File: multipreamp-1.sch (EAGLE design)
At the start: 132 parts, among them Q1 J201, Q2 J201, Q3 J201, Q4 J201, Q5 2N5088, Q6 J201, Q7 J201, Q8 J201

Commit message: Adicao de filtros RC na alimentacao (esquematico e layout)
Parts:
- added C43: (no value), rcl:CPOL-EUE2.5-6
- added R49, R50: (no value), rcl:R-US_0207/7
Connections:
- new net 9V_1: C3.1, C37.1, C6.+, Q5.C, Q8.D, R23.A, R29.A, R31.1, R49.2, R50.1
- new net N$44: JP+.1, R49.1
- net GND: now also C43.-
- net V+: now also C43.+, R50.2; no longer C3.1, C37.1, C6.+, JP+.1, Q5.C, Q8.D, R23.A, R29.A, R31.1
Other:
- moved on the sheet: C26, C27, C3, C38, C6, C7, JP+, JP-, Q6, R40, R7

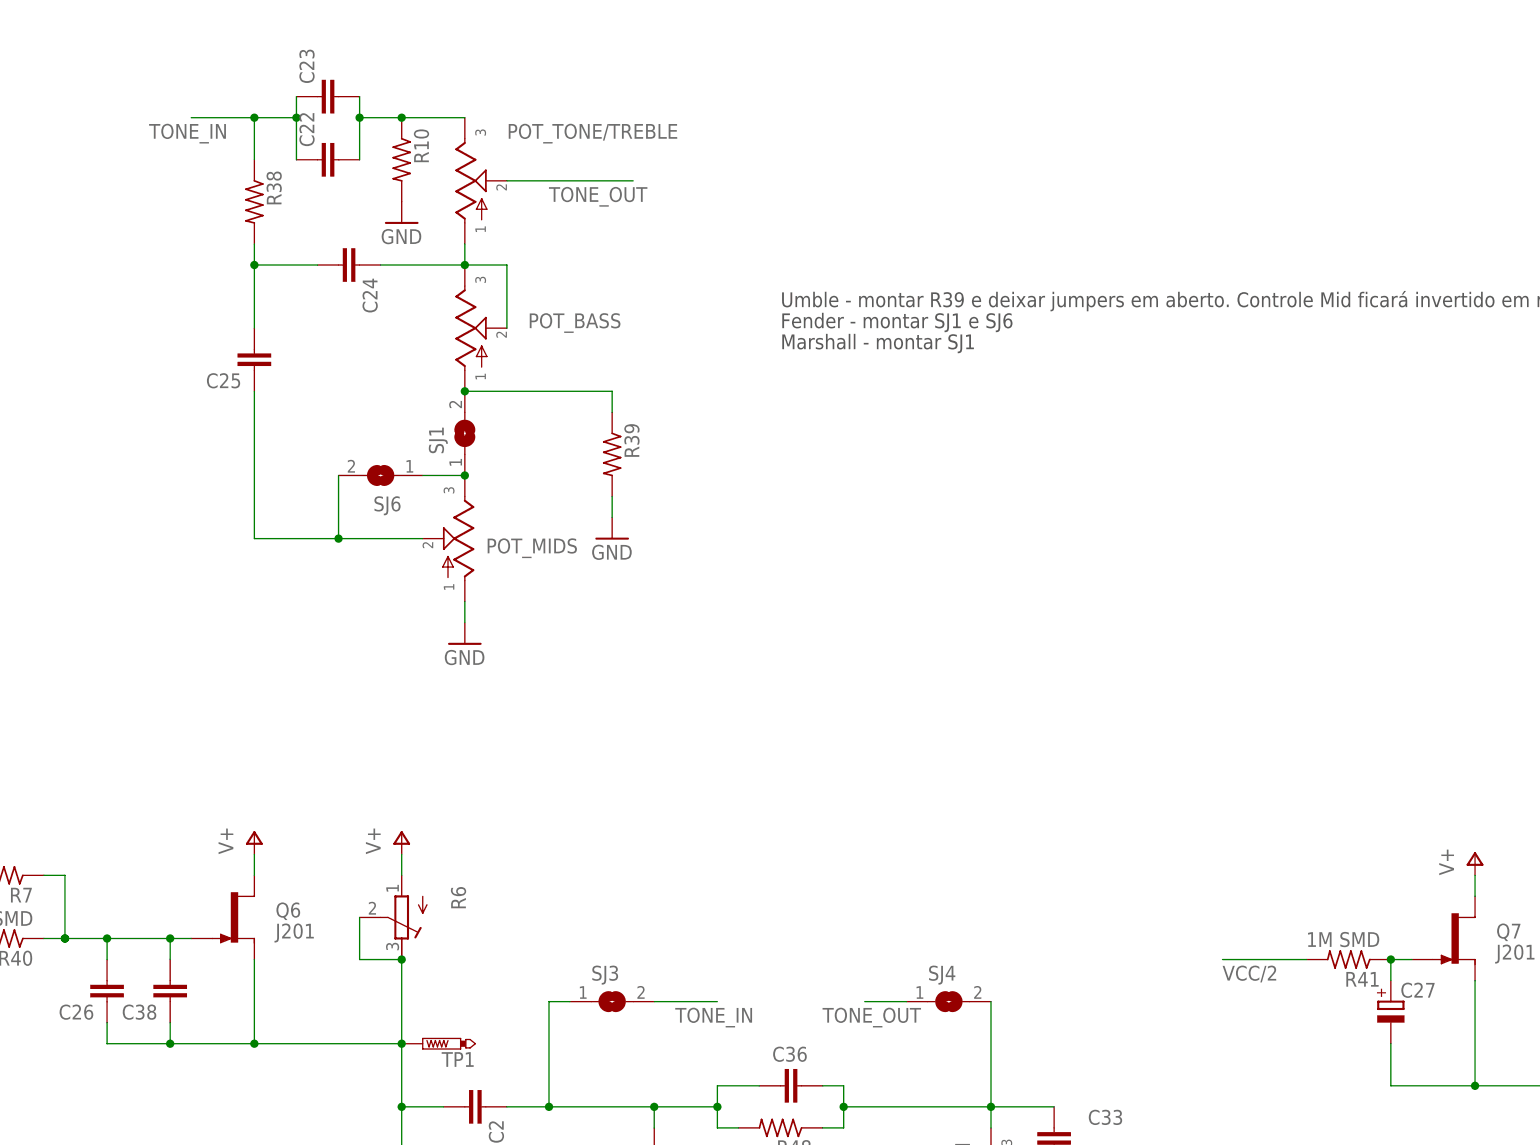
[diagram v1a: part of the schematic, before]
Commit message: Alteracao no layout - troca de posicao entre pots de agudos e graves
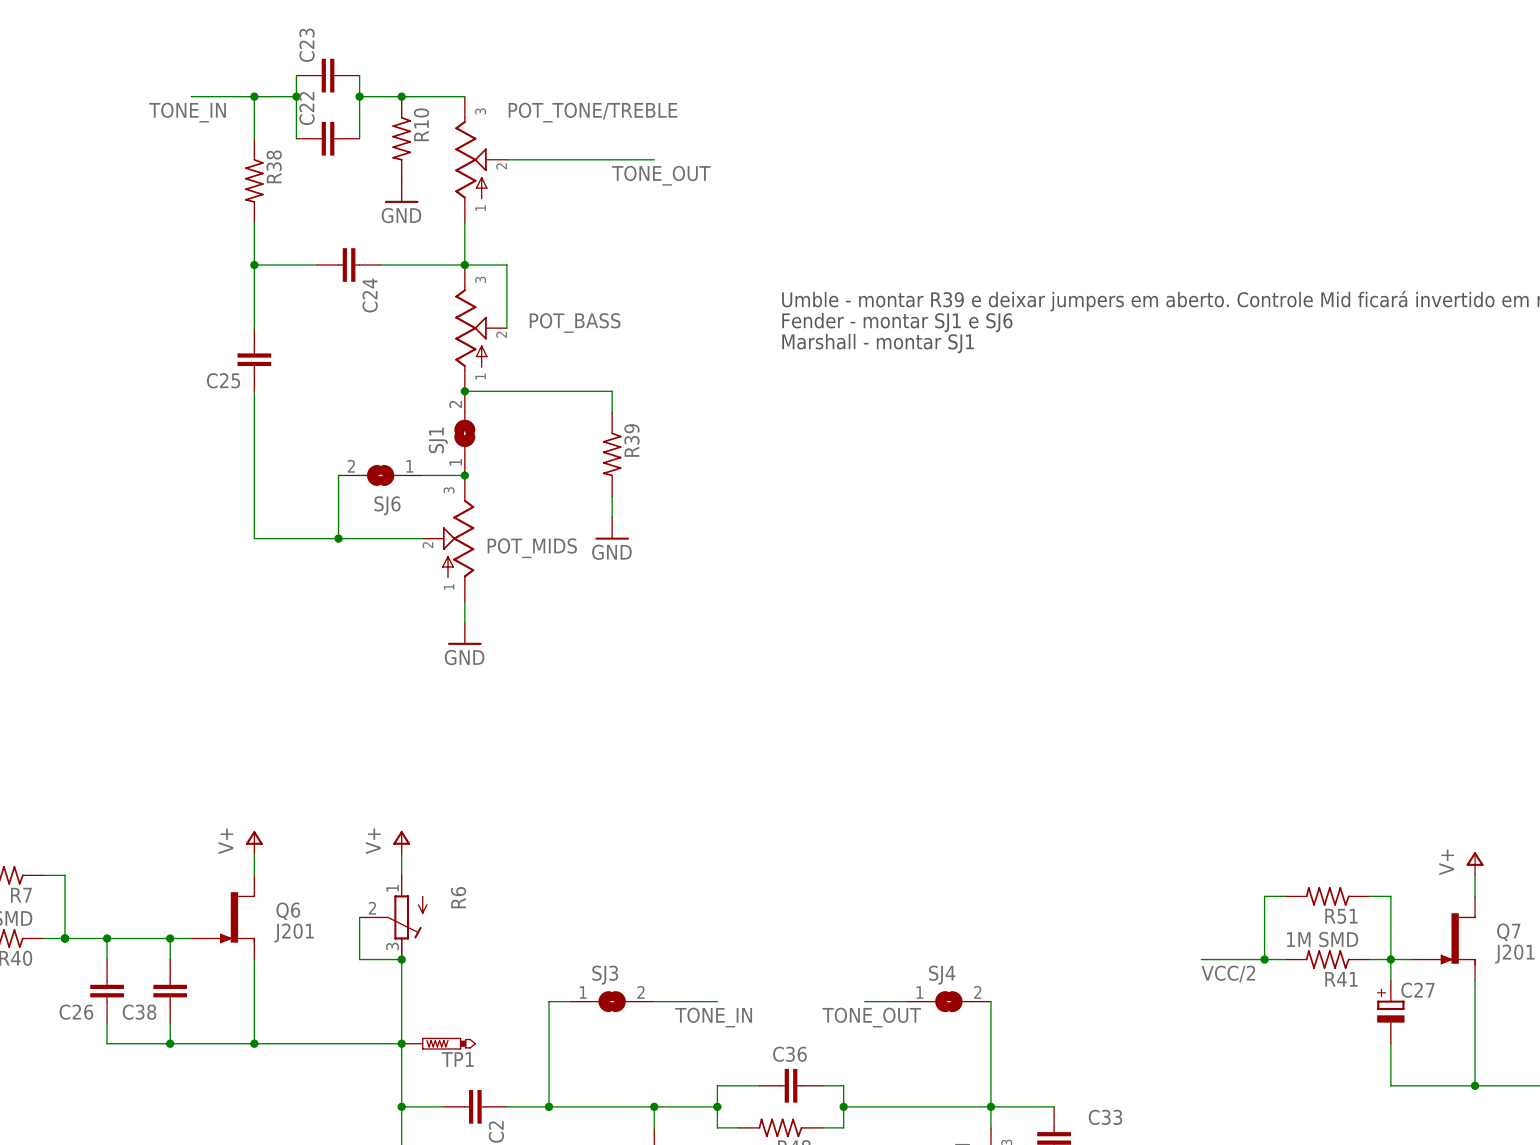
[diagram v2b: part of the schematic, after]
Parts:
- added R51: (no value), rcl:R-US_0207/5V
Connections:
- net N$40: now also R51.1
- net VCC/2: now also R51.2
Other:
- moved on the sheet: C22, C23, POT_TONE/TREBLE, R10, R38, R41

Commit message: Alteracoes no layout - troca de encapsulamentos Renumeracao dos componentes
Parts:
- removed JP+, JP-, JP_BRT2, JP_IN: (no value), pinhead:PINHD-1X1
- removed POT_TONE/TREBLE: (no value), gm-pots:POTPCB
- added JP10, JP13, JP4, JP8: (no value), pinhead:PINHD-1X1
- added POT_TREBLE/TONE: (no value), gm-pots:POTPCB
- C1, C22, C26, C33: device rcl:C-EU025-025X050 -> rcl:CPOL-EUE2.5-6
- C11, C20, C24, C25, C35, C36, C8: device rcl:C-EU050-025X075 -> rcl:C-EU025-025X050
- C13, C15, C38, C40, C41, C42: device rcl:C-EU025-025X050 -> rcl:C-EU050-025X075
- C14, C37: device rcl:C-EU050-025X075 -> rcl:CPOL-EUE2.5-6
- C2, C4, C5: value (none) -> 100n SMD; device rcl:C-EU050-025X075 -> rcl:C-EUC0805
- C27, C29, C32, C43: device rcl:CPOL-EUE2.5-6 -> rcl:C-EU050-025X075
- C28: value 100n SMD -> (none); device rcl:C-EUC0805 -> rcl:C-EU025-025X050
- C3: value 100n SMD -> (none); device rcl:C-EUC0805 -> rcl:CPOL-EUE2.5-6
- C30, C31: device rcl:CPOL-EUE2.5-6 -> rcl:C-EU025-025X050
- C7: value 100n SMD -> (none); device rcl:C-EUC0805 -> rcl:C-EU050-025X075
- Q5: value 2N5088 -> J201; device gm-trans:2N5088 -> gm-trans:J201
- Q8: value J201 -> 2N5088; device gm-trans:J201 -> gm-trans:2N5088
- R10, R22, R26, R30, R36, R5: value (none) -> 1M SMD; device rcl:R-US_0207/7 -> rcl:R-US_R0805
- R11: device rcl:R-US_R0805 -> rcl:R-US_0207/7
- R12: value 1M SMD -> (none); device rcl:R-US_R0805 -> rcl:R-TRIMM64W
- R17, R23, R29: device rcl:R-TRIMM64W -> rcl:R-US_0207/7
- R18, R24, R40, R41, R45: value 1M SMD -> (none); device rcl:R-US_R0805 -> rcl:R-US_0207/7
- R19, R2, R46, R51: device rcl:R-US_0207/5V -> rcl:R-US_0207/7
- R21: device rcl:R-US_0207/7 -> rcl:R-US_R0805
- R25, R31, R9: device rcl:R-US_0207/7 -> rcl:R-US_0207/5V
- R27, R33, R39: device rcl:R-US_0207/7 -> rcl:R-TRIMM64W
- R3: value 1M SMD -> 10k SMD
- R4: value (none) -> 10k SMD; device rcl:R-US_0207/7 -> rcl:R-US_R0805
- R42, R43: value 10k SMD -> (none); device rcl:R-US_R0805 -> rcl:R-US_0207/7
- R6: device rcl:R-TRIMM64W -> rcl:R-US_0207/2V
- R7: value (none) -> 1M SMD; device rcl:R-US_0207/5V -> rcl:R-US_R0805
- R8: device rcl:R-US_0207/7 -> rcl:R-US_0207/2V
- renumbered JP_BRT1 to JP5, JP_OUT to JP12
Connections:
- net 9V_1: now also C1.+, C2.1, C29.1, Q7.D, Q8.C, R1.2, R2.1, R33.A, R39.A, R43.1; no longer C3.1, C37.1, C6.+, Q5.C, Q8.D, R23.A, R29.A, R31.1, R49.2, R50.1
- net GND: now also C1.-, C2.2, C23.1, C24.1, C26.-, C28.1, C3.-, C30.1, C33.-, C35.1, C37.-, C39.1, C4.2, C42.1, C5.2, C8.1, JP13.1, JP2.1, JP4.1, R14.1, R15.1, R17.1, R18.2, R20.2, R21.1, R23.1, R29.1, R30.1, R31.1, R35.1, R36.1, R4.2, R41.1, R46.2, R47.2, R50.1, R6.1, R7.1; no longer C1.1, C12.1, C13.1, C15.1, C16.1, C17.1, C21.1, C28.2, C29.-, C3.2, C30.-, C31.-, C32.-, C43.-, C7.2, C9.1, JP-.1, JP9.1, JP_BRT2.1, R10.2, R11.1, R12.1, R13.1, R16.1, R18.1, R19.1, R2.1, R24.1, R25.1, R28.1, R3.1, R33.2, R34.2, R39.2, R43.2, R45.1, R46.1, R47.1
- net N$1: now also C14.-, R15.2; no longer C4.2, R5.2
- net N$10: now also C43.2, R51.2; no longer C5.2, R9.2
- net N$11: now also C19.1, C20.2, R19.1; no longer C33.2, C36.1, R48.1
- net N$12: now also R21.2; no longer R11.2
- net N$13: now also C21.1, R22.2, R23.2, R24.2; no longer C8.1, R12.2, R13.2, R14.2
- net N$14: now also C43.1, JP10.1; no longer C5.1, JP7.1
- net N$15: now also C22.-, C27.2, JP7.1, Q3.S, Q4.D, R27.E, R27.S; no longer C11.2, C27.-, JP1.1, Q2.D, Q7.S, R17.E, R17.S
- net N$16: now also C25.1, C26.+, Q4.S, R28.2; no longer C30.+, C40.1, Q2.S, R15.2
- net N$17: now also R28.1, R29.2; no longer R15.1, R16.2
- net N$18: now also C27.1, R30.2, R31.2, R32.2; no longer C11.1, R18.2, R19.2, R20.2
- net N$19: now also C28.2, C30.2, C31.2, Q5.G, R32.1; no longer C12.2, C13.2, C41.2, Q3.G, R20.1
- net N$2: now also C12.1, C14.+, Q2.S, R13.2; no longer C39.1, C4.1, Q1.S, R4.2
- net N$20: now also C31.1, C33.+, Q5.S, R34.2; no longer C31.+, C41.1, Q3.S, R21.2
- net N$21: now also R34.1, R35.2; no longer R21.1, R22.2
- net N$22: now also C29.2, C32.2, Q5.D, R33.E, R33.S; no longer C14.2, C37.2, Q3.D, R23.E, R23.S
- net N$23: now also C38.1, R42.1, R43.2, R45.1; no longer C18.1, R30.1, R31.2, R32.1
- net N$24: now also C32.1, R36.2, R37.2, R38.2; no longer C14.1, R24.2, R25.2, R26.2
- net N$25: now also C34.2, C35.2, C36.2, Q6.G, R38.1; no longer C15.2, C16.2, C42.2, Q4.G, R26.1
- net N$26: now also C36.1, C37.+, Q6.S, R40.2; no longer C32.+, C42.1, Q4.S, R27.2
- net N$27: now also R40.1, R41.2; no longer R27.1, R28.2
- net N$28: now also JP8.1, Q6.D, Q7.G, R39.E, R39.S, SJ5.1; no longer JP2.1, Q4.D, Q8.G, R29.E, R29.S, SJ2.1
- net N$29: now also JP9.1, R42.2, SJ5.2; no longer JP3.1, R30.2, SJ2.2
- net N$3: now also C20.1, C21.2; no longer C33.1, C8.2
- net N$30: now also C39.2, Q8.B, R45.2; no longer C17.2, Q5.B, R32.2
- net N$31: now also C38.2, C40.1, Q8.E, R46.1; no longer C18.2, C19.1, Q5.E, R33.1
- net N$32: now also C40.2, C41.1, R47.1, R48.1; no longer C19.2, C20.1, R34.1, R35.1
- net N$33: now also C42.2, R48.2, R49.1; no longer C21.2, R35.2, R36.1
- net N$34: now also R13.1, R14.2; no longer R4.1, R44.2
- net N$36: now also C15.2, C18.2, R16.2; no longer C24.2, C25.2, R38.2
- net N$37: now also SJ2.1, SJ3.1; no longer SJ1.1, SJ6.1
- net N$38: now also C7.1, JP3.1, R5.2, R6.2; no longer C35.1, JP_IN.1, R45.2, R46.2
- net N$39: now also C13.1, C19.2, R17.2, R19.2, SJ1.1; no longer C2.1, C36.2, R47.2, R48.2, SJ3.1
- net N$4: now also C10.2, C12.2, C8.2, Q2.G, R11.2; no longer C1.2, C34.2, C39.2, Q1.G, R1.2
- net N$40: now also C22.+, Q3.G, R25.1, R26.1; no longer C27.+, Q7.G, R41.1, R51.1
- net N$42: now also C23.2, C24.2, C25.2, Q4.G, R24.1; no longer C10.2, C40.2, C9.2, Q2.G, R14.1
- net N$43: now also R20.1, SJ3.2; no longer R39.1, SJ1.2
- net N$44: now also JP1.1, R1.1; no longer JP+.1, R49.1
- net N$5: now also C7.2, R11.1, R7.2, R8.2; no longer C35.2, R1.1, R2.2, R3.2
- net N$6: now also C15.1, SJ2.2; no longer C25.1, SJ6.2
- net N$7: now also C11.2, C9.2, Q1.G, R10.1, R9.1; no longer C26.2, C38.2, Q6.G, R40.1, R7.1
- net N$8: now also C11.1, C13.2, C9.1, Q1.S, Q2.D, R12.E, R12.S; no longer C2.2, C26.1, C38.1, Q1.D, Q6.S, R6.E, R6.S
- net N$9: now also C41.2, R49.2, R50.2, R51.1, SJ6.2; no longer C20.2, R36.2, R37.2, R9.1, SJ5.2
- net TONE/TREBLE_1: now also C18.1, POT_TREBLE/TONE.1; no longer C24.1, POT_TONE/TREBLE.1
- net TONE/TREBLE_3: now also C16.2, C17.2, POT_TREBLE/TONE.3, R18.1; no longer C22.2, C23.2, POT_TONE/TREBLE.3, R10.1
- net TONE_IN: now also C16.1, C17.1, Q7.S, R16.1, R44.2, SJ1.2; no longer C22.1, C23.1, Q8.S, R38.1, R8.2, SJ3.2
- net TONE_OUT: now also POT_TREBLE/TONE.2, SJ6.1; no longer POT_TONE/TREBLE.2, SJ5.1
- net V+: now also C3.+, C4.1, Q1.D, Q3.D, R12.A, R2.2, R27.A, R3.1; no longer C43.+, C7.1, Q6.D, Q7.D, R17.A, R42.1, R50.2, R6.A
- net VCC/2: now also C5.1, C6.+, R10.2, R25.2, R26.2, R3.2, R4.1, R9.2; no longer C28.1, C29.+, R40.2, R41.2, R42.2, R43.1, R51.2, R7.2
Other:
- note added: "Ponto para chave Clean/Dirt Azabache"
- note added: "Pontos apenas para chave Clean/Dirt no Azabache, se montado"
- note removed: "Ponto JP1 para chave Clean/Dirt Azabache"
- note removed: "Pontos JP2 e JP3 apenas para chave Clean/Dirt no Azabache, se montado"
- moved on the sheet: C10, C11, C12, C13, C15, C16, C17, C18, C19, C2, C20, C21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

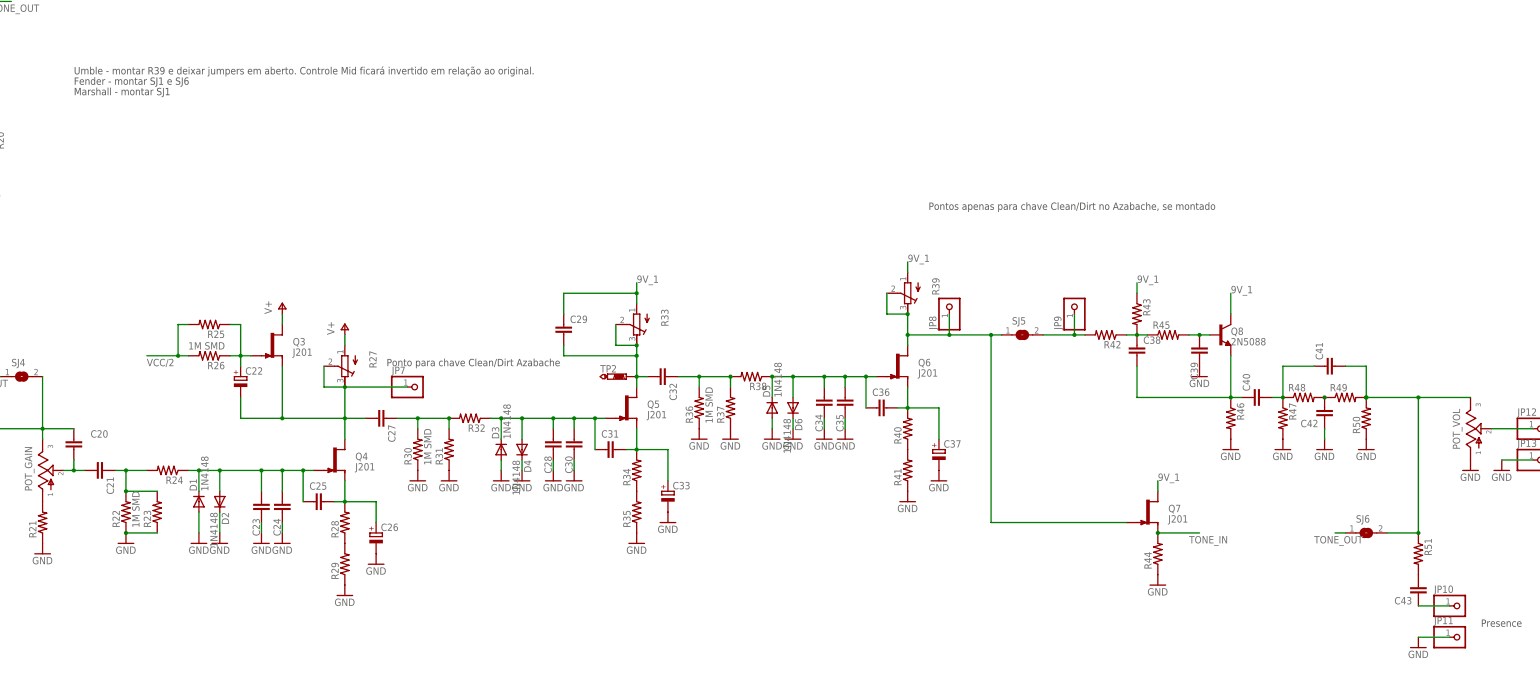
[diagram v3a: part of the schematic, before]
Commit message: Alteracao no esquematico e layout - adicao de jumper para selecao da ligacao na saida do buffer JFET
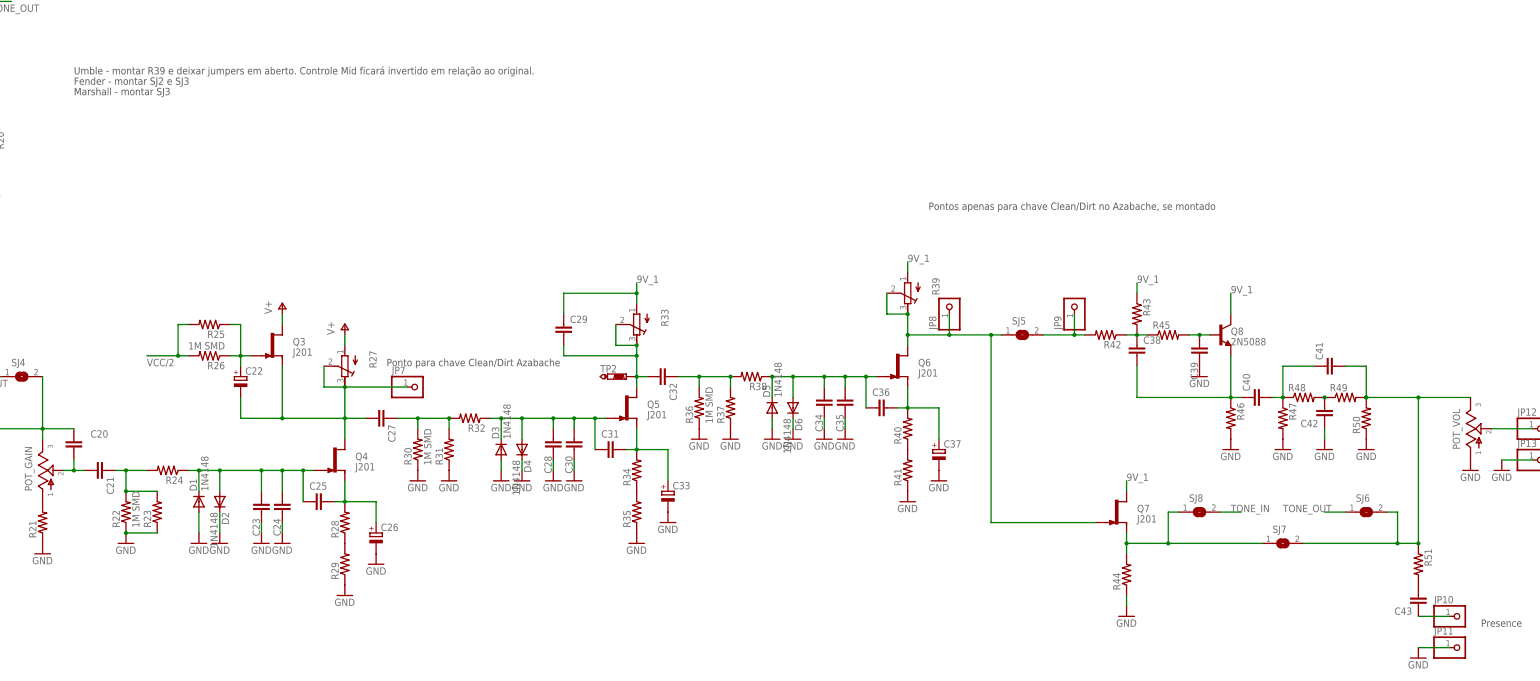
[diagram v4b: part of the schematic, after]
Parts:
- added SJ7, SJ8: (no value), jumper:SJ
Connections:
- new net N$45: Q7.S, R44.2, SJ7.1, SJ8.1
- net N$9: now also SJ7.2
- net TONE_IN: now also SJ8.2; no longer Q7.S, R44.2
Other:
- note added: "Fender - montar SJ2 e SJ3"
- note added: "Marshall - montar SJ3"
- note removed: "Fender - montar SJ1 e SJ6"
- note removed: "Marshall - montar SJ1"
- moved on the sheet: C43, JP10, JP11, Q7, R44, R51, SJ6
